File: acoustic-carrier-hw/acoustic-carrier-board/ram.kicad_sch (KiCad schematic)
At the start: 15 parts, among them IC1 ECP5-BGA256, IC2 MT41K256M16TW-107_P

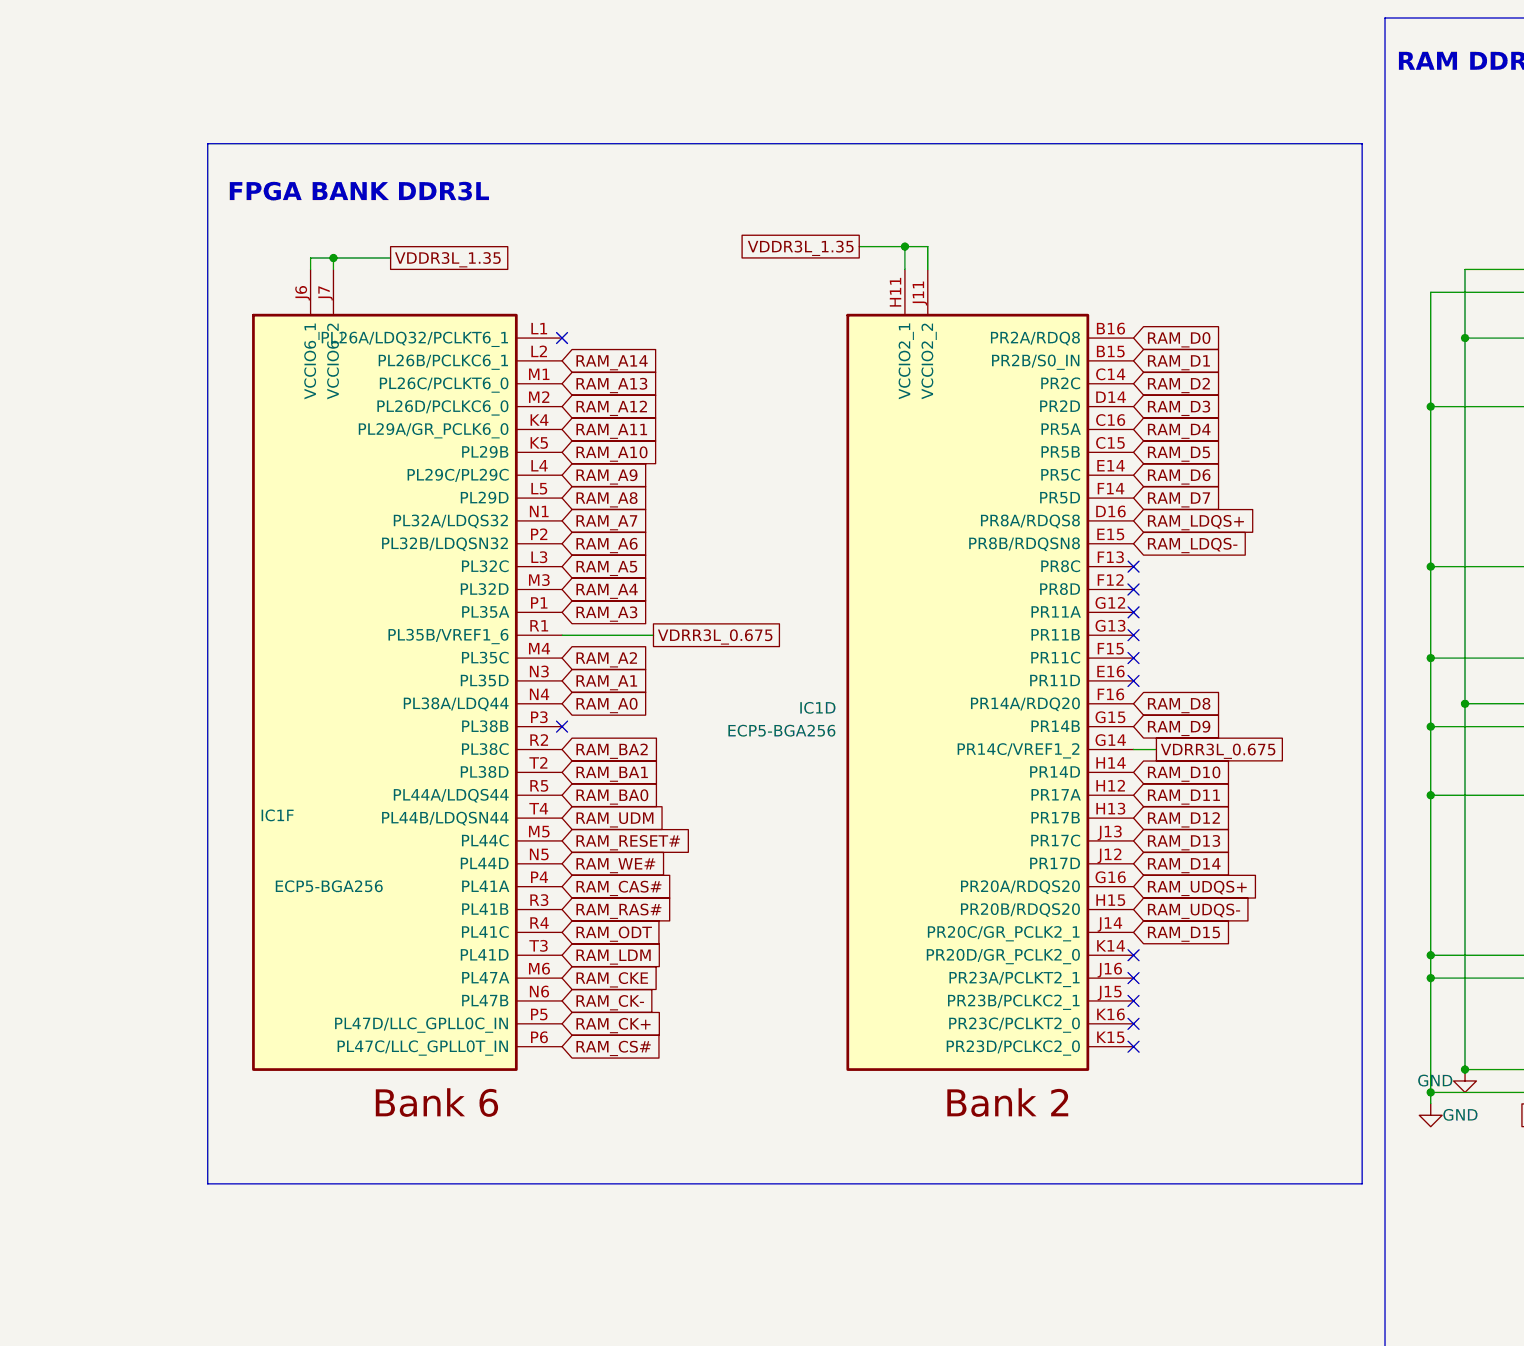
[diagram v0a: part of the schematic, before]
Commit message: [carrier] Fixed ERC errors and fpga-footprints (next) ) add extra pin functionality to 2 remaining banks, perform schematic checks
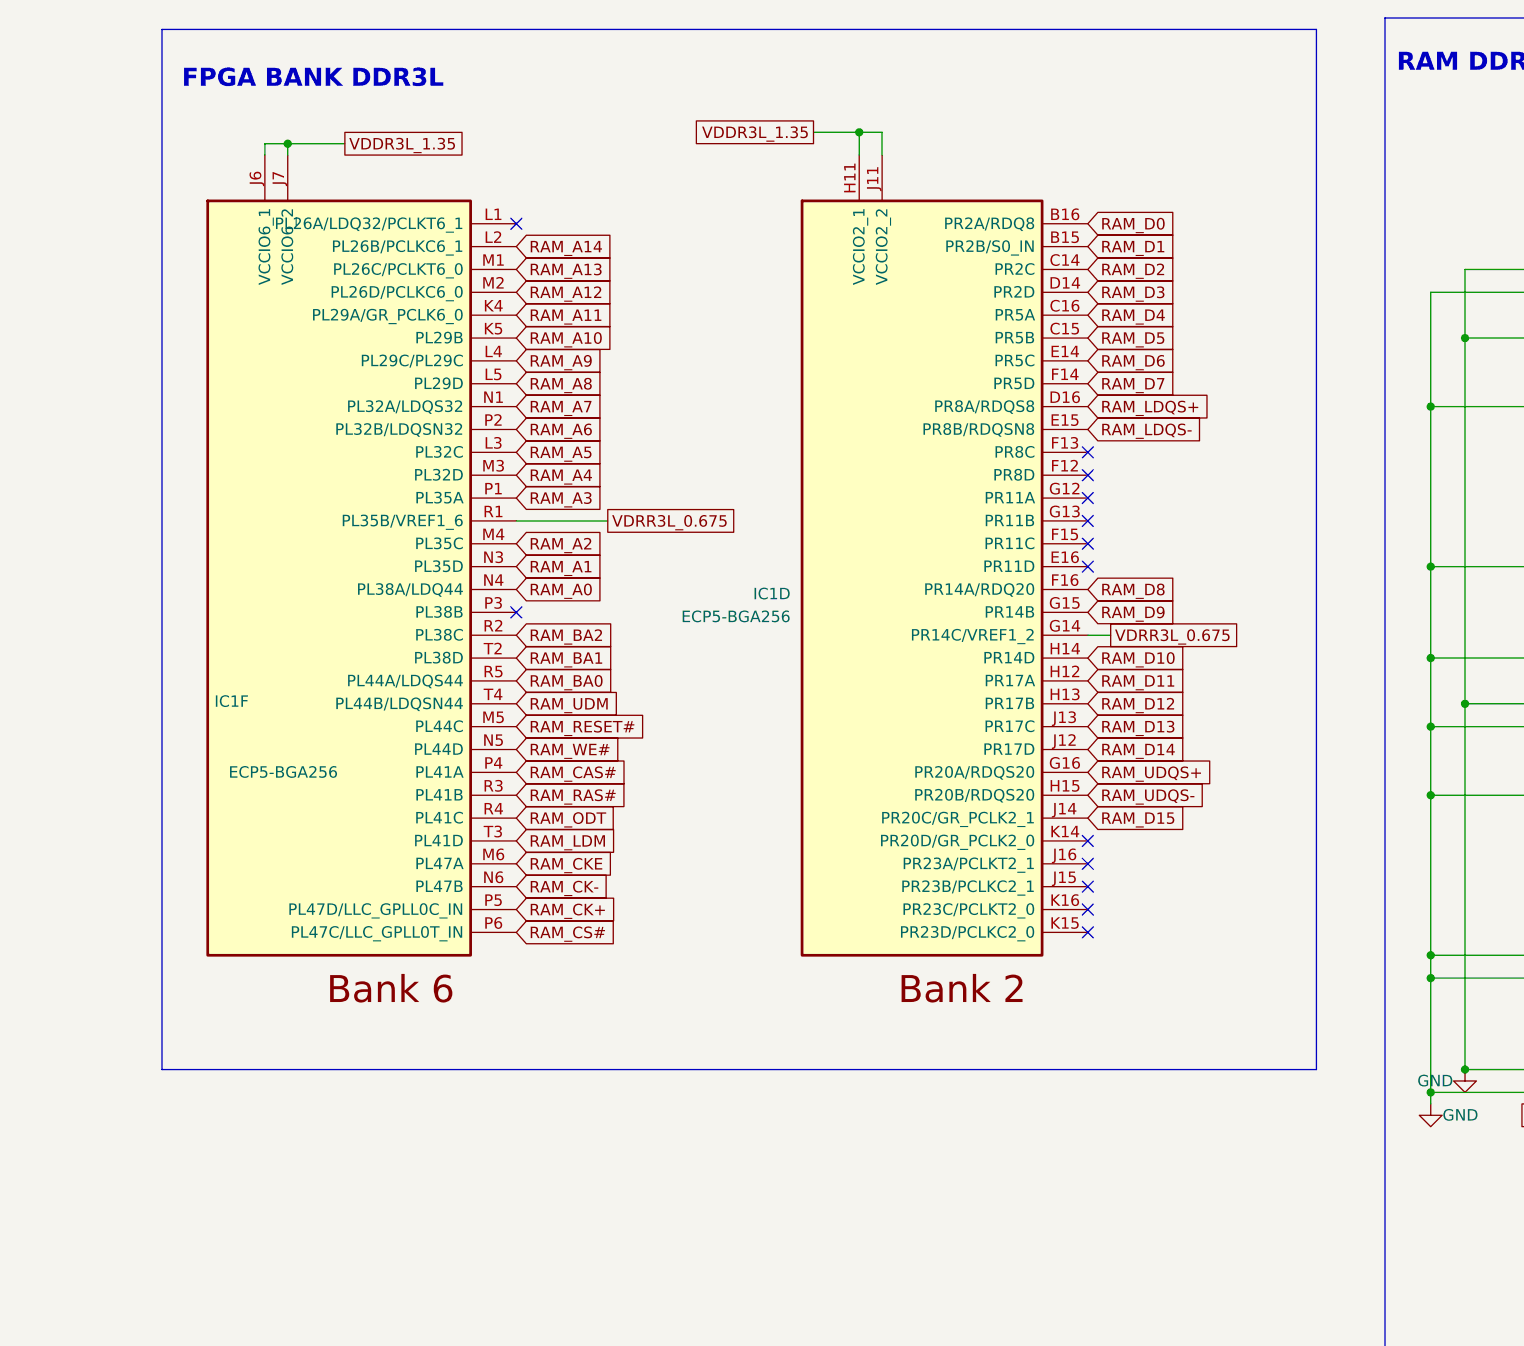
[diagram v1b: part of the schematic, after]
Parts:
- IC1: Part Number LFE5U-25F-6BG256C -> (none)
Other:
- moved on the sheet: IC1D, IC1F

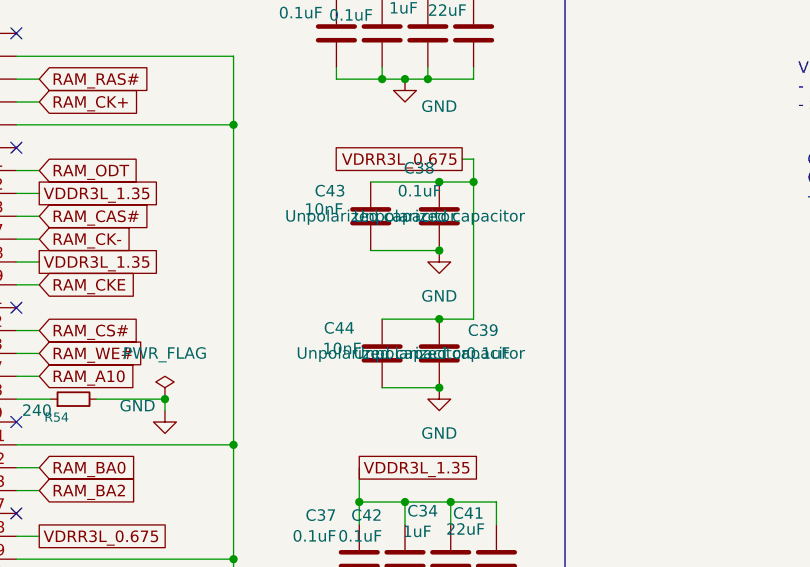
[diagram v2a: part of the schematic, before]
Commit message: [carrier] Chose amplifier, changed adc voltage range (next) change commmon mode source, add decoupling, add buffering to common mode
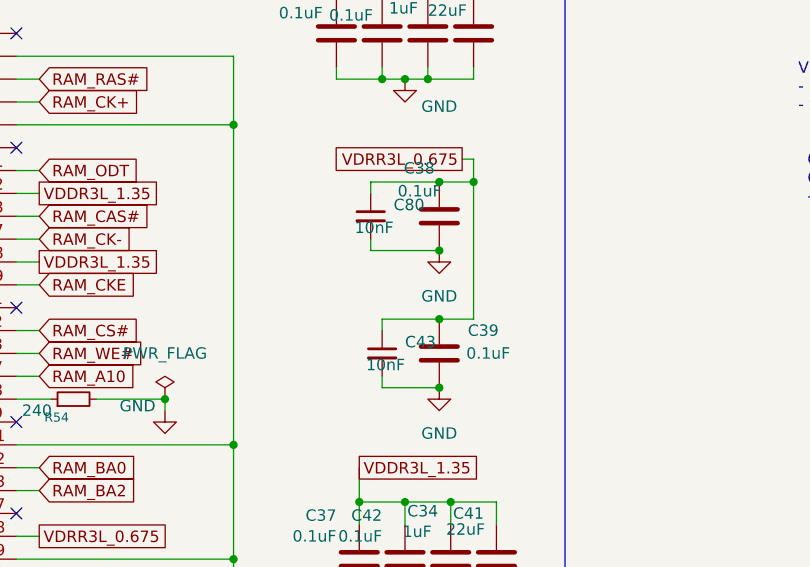
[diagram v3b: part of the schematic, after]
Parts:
- removed C43, C44: 10nF, Capacitor_SMD:C_0402_1005Metric, symbol Device:C
- added C43, C80: 10nF, Capacitor_SMD:C_0402_1005Metric, symbol Device:C_Small
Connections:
- net GND: now also C43.2, C80.2
- net VDRR3L_0.675: now also C43.1, C80.1
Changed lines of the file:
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@@
 	(wire
 		(pts
+			(xy 262.89 50.8) (xy 262.89 52.07)
+		)
+		(stroke
+			(width 0)
+			(type default)
+		)
+	)
+	(wire
+		(pts
 			(xy 247.65 104.14) (xy 247.65 116.84)
 		)
@@
 	(wire
 		(pts
+			(xy 262.89 44.45) (xy 262.89 45.72)
+		)
+		(stroke
+			(width 0)
+			(type default)
+		)
+	)
+	(wire
+		(pts
 			(xy 185.42 63.5) (xy 187.96 63.5)
 		)
@@
 	(wire
 		(pts
+			(xy 264.16 59.69) (xy 264.16 60.96)
+		)
+		(stroke
+			(width 0)
+			(type default)
+		)
+	)
+	(wire
+		(pts
 			(xy 165.1 40.64) (xy 187.96 40.64)
 		)
@@
 	(wire
 		(pts
+			(xy 264.16 66.04) (xy 264.16 67.31)
+		)
+		(stroke
+			(width 0)
+			(type default)
+		)
+	)
+	(wire
+		(pts
 			(xy 223.52 63.5) (xy 226.06 63.5)
 		)
@@
 	)
 	(symbol
-		(lib_id "Device:C")
-		(at 262.89 48.26 0)
-		(mirror y)
-		(unit 1)
-		(exclude_from_sim no)
-		(in_bom yes)
-		(on_board yes)
-		(dnp no)
-		(property "Reference" "C43"
-			(at 260.096 45.466 0)
-			(effects
-				(font
-					(size 1.27 1.27)
-				)
-				(justify left)
-			)
-		)
-		(property "Value" "10nF"
-			(at 259.842 47.498 0)
-			(effects
-				(font
-					(size 1.27 1.27)
-				)
-				(justify left)
-			)
-		)
-		(property "Footprint" "Capacitor_SMD:C_0402_1005Metric"
-			(at 261.9248 52.07 0)
-			(effects
-				(font
-					(size 1.27 1.27)
-				)
-				(hide yes)
-			)
-		)
-		(property "Datasheet" "~"
-			(at 262.89 48.26 0)
-			(effects
-				(font
-					(size 1.27 1.27)
-				)
-				(hide yes)
-			)
-		)
-		(property "Description" "Unpolarized capacitor"
-			(at 262.89 48.26 0)
-			(effects
-				(font
-					(size 1.27 1.27)
-				)
-			)
-		)
-		(property "LCSC Part Number" ""
-			(at 262.89 46.99 0)
-			(effects
-				(font
-					(size 1.27 1.27)
-				)
-				(hide yes)
-			)
-		)
-		(property "Manufacturing Part Number" ""
-			(at 262.89 48.26 0)
-			(effects
-				(font
-					(size 1.27 1.27)
-				)
-				(hide yes)
-			)
-		)
-		(property "LPN" "CL05B103KB5NNNC"
-			(at 262.89 48.26 0)
-			(effects
-				(font
-					(size 1.27 1.27)
-				)
-				(hide yes)
-			)
-		)
-		(property "MPN" "C15195"
-			(at 262.89 48.26 0)
-			(effects
-				(font
-					(size 1.27 1.27)
-				)
-				(hide yes)
-			)
-		)
-		(property "Part Number" ""
-			(at 262.89 48.26 0)
-			(effects
-				(font
-					(size 1.27 1.27)
-				)
-				(hide yes)
-			)
-		)
-		(property "SN-DK" ""
-			(at 262.89 48.26 0)
-			(effects
-				(font
-					(size 1.27 1.27)
-				)
-				(hide yes)
-			)
-		)
-		(property "Sim.Pin" ""
-			(at 262.89 48.26 0)
-			(effects
-				(font
-					(size 1.27 1.27)
-				)
-				(hide yes)
-			)
-		)
-		(property "LCSC Part" ""
-			(at 262.89 48.26 0)
-			(effects
-				(font
-					(size 1.27 1.27)
-				)
-				(hide yes)
-			)
-		)
-		(pin "1"
-		)
-		(pin "2"
-		)
-		(instances
-			(project "acoustic-carrier-board"
-				(path "/25b015c9-ab13-4427-b72c-b6f348597100/f2b9f5c5-2b83-49a1-9584-962bb926f77f"
-					(reference "C43")
-					(unit 1)
-				)
-			)
-		)
-	)
-	(symbol
 		(lib_id "power:PWR_FLAG")
 		(at 240.03 68.58 0)
@@
 					(size 1.27 1.27)
 				)
+				(hide yes)
 			)
 		)
@@
 					(size 1.27 1.27)
 				)
+				(hide yes)
 			)
 		)
@@
 	)
 	(symbol
+		(lib_id "Device:C_Small")
+		(at 264.16 63.5 0)
+		(unit 1)
+		(exclude_from_sim no)
+		(in_bom yes)
+		(on_board yes)
+		(dnp no)
+		(fields_autoplaced yes)
+		(property "Reference" "C43"
+			(at 266.7 62.2362 0)
+			(effects
+				(font
+					(size 1.27 1.27)
+				)
+				(justify left)
+			)
+		)
+		(property "Value" "10nF"
+			(at 266.7 64.7762 0)
+			(effects
+				(font
+					(size 1.27 1.27)
+				)
+				(justify right)
+			)
+		)
+		(property "Footprint" "Capacitor_SMD:C_0402_1005Metric"
+			(at 264.16 63.5 0)
+			(effects
+				(font
+					(size 1.27 1.27)
+				)
+				(hide yes)
+			)
+		)
+		(property "Datasheet" "~"
+			(at 264.16 63.5 0)
+			(effects
+				(font
+					(size 1.27 1.27)
+				)
+				(hide yes)
+			)
+		)
+		(property "Description" "Unpolarized capacitor"
+			(at 264.16 63.5 0)
+			(effects
+				(font
+					(size 1.27 1.27)
+				)
+				(hide yes)
+			)
+		)
+		(property "LPN" "CL05B103KB5NNNC"
+			(at 264.16 63.5 0)
+			(effects
+				(font
+					(size 1.27 1.27)
+				)
+				(hide yes)
+			)
+		)
+		(property "MPN" "C15195"
+			(at 264.16 63.5 0)
+			(effects
+				(font
+					(size 1.27 1.27)
+				)
+				(hide yes)
+			)
+		)
+		(pin "1"
+		)
+		(pin "2"
+		)
+		(instances
+			(project "acoustic-carrier-board"
+				(path "/25b015c9-ab13-4427-b72c-b6f348597100/f2b9f5c5-2b83-49a1-9584-962bb926f77f"
+					(reference "C43")
+					(unit 1)
+				)
+			)
+		)
+	)
+	(symbol
 		(lib_id "power:GND")
 		(at 165.1 129.54 0)
@@
 	)
 	(symbol
-		(lib_id "Device:C")
-		(at 264.16 63.5 0)
-		(mirror y)
+		(lib_id "Device:C_Small")
+		(at 262.89 48.26 0)
 		(unit 1)
 		(exclude_from_sim no)
@@
 		(on_board yes)
 		(dnp no)
-		(property "Reference" "C44"
-			(at 261.112 60.706 0)
+		(fields_autoplaced yes)
+		(property "Reference" "C80"
+			(at 265.43 46.9962 0)
 			(effects
 				(font
@@
 		)
 		(property "Value" "10nF"
-			(at 261.874 62.992 0)
+			(at 265.43 49.5362 0)
 			(effects
 				(font
 					(size 1.27 1.27)
 				)
-				(justify left)
+				(justify right)
 			)
 		)
 		(property "Footprint" "Capacitor_SMD:C_0402_1005Metric"
-			(at 263.1948 67.31 0)
+			(at 262.89 48.26 0)
 			(effects
 				(font
@@
 		)
 		(property "Datasheet" "~"
-			(at 264.16 63.5 0)
+			(at 262.89 48.26 0)
 			(effects
 				(font
@@
 		)
 		(property "Description" "Unpolarized capacitor"
-			(at 264.16 63.5 0)
-			(effects
-				(font
-					(size 1.27 1.27)
-				)
-			)
-		)
-		(property "LCSC Part Number" ""
-			(at 264.16 62.23 0)
-			(effects
-				(font
-					(size 1.27 1.27)
-				)
-				(hide yes)
-			)
-		)
-		(property "Manufacturing Part Number" ""
-			(at 264.16 63.5 0)
+			(at 262.89 48.26 0)
 			(effects
 				(font
@@
 		)
 		(property "LPN" "CL05B103KB5NNNC"
-			(at 264.16 63.5 0)
+			(at 262.89 48.26 0)
 			(effects
 				(font
@@
 		)
 		(property "MPN" "C15195"
-			(at 264.16 63.5 0)
-			(effects
-				(font
-					(size 1.27 1.27)
-				)
-				(hide yes)
-			)
-		)
-		(property "Part Number" ""
-			(at 264.16 63.5 0)
-			(effects
-				(font
-					(size 1.27 1.27)
-				)
-				(hide yes)
-			)
-		)
-		(property "SN-DK" ""
-			(at 264.16 63.5 0)
-			(effects
-				(font
-					(size 1.27 1.27)
-				)
-				(hide yes)
-			)
-		)
-		(property "Sim.Pin" ""
-			(at 264.16 63.5 0)
-			(effects
-				(font
-					(size 1.27 1.27)
-				)
-				(hide yes)
-			)
-		)
-		(property "LCSC Part" ""
-			(at 264.16 63.5 0)
+			(at 262.89 48.26 0)
 			(effects
 				(font
@@
 		)
 		(instances
-			(project "acoustic-carrier-board"
+			(project ""
 				(path "/25b015c9-ab13-4427-b72c-b6f348597100/f2b9f5c5-2b83-49a1-9584-962bb926f77f"
-					(reference "C44")
+					(reference "C80")
 					(unit 1)
 				)
